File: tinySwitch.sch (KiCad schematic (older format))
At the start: 8 parts, among them J1 Vout Vin Gnd, J2 Raspberry Pi Input, K1 1 Channel Relay, SW1 Power Button, U1 Digispark Tiny85

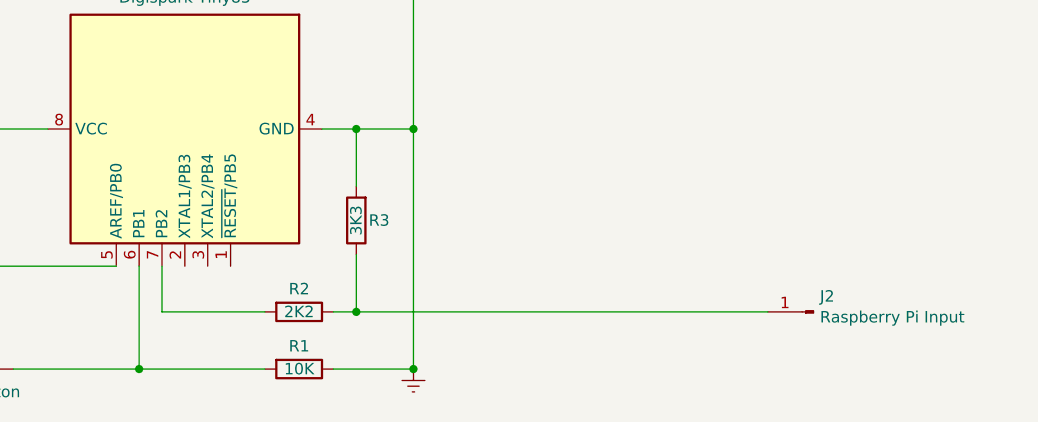
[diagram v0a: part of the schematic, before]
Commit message: Adding RPi detection line (Input)
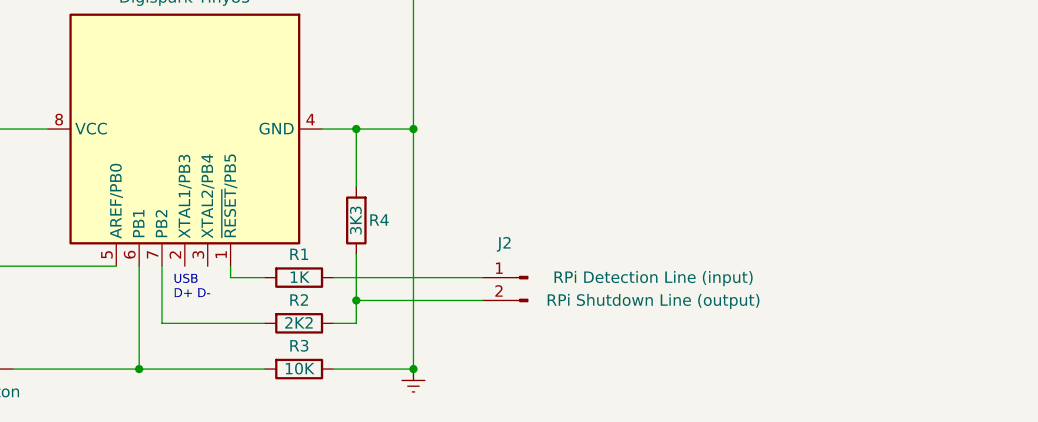
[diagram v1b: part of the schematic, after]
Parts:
- removed J2: Raspberry Pi Input, symbol Connector:Conn_01x01_Male
- added J2: Conn_01x02_Male, symbol Connector:Conn_01x02_Male
- added R1: 1K, symbol Device:R
- renumbered R1 to R3, R3 to R4
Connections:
- net at U1.1 (~RESET~/PB5): now also R1.2
- net at R2.1, R4.1: now also J2.2 (Pin_2)
- new net: J2.1 (Pin_1), R1.1
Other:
- note added: "USB\nD+ D-"
- moved on the sheet: R2
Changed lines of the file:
@@
 $EndComp
 $Comp
-L Device:R R1
+L Device:R R3
 U 1 1 5FBB20BE
 P 6600 4400
-F 0 "R1" V 6500 4400 50  0000 C CNN
+F 0 "R3" V 6500 4400 50  0000 C CNN
 F 1 "10K" V 6600 4400 50  0000 C CNN
 F 2 "" V 6530 4400 50  0001 C CNN
@@
 Connection ~ 7100 3350
 Wire Wire Line
-	6000 3950 6000 4150
+	6000 3950 6000 4200
 Wire Wire Line
-	6000 4150 6450 4150
+	6000 4200 6450 4200
 $Comp
 L Device:R R2
 U 1 1 5FBBB646
-P 6600 4150
-F 0 "R2" V 6500 4150 50  0000 C CNN
-F 1 "2K2" V 6600 4150 50  0000 C CNN
-F 2 "" V 6530 4150 50  0001 C CNN
-F 3 "~" H 6600 4150 50  0001 C CNN
-	1    6600 4150
+P 6600 4200
+F 0 "R2" V 6500 4200 50  0000 C CNN
+F 1 "2K2" V 6600 4200 50  0000 C CNN
+F 2 "" V 6530 4200 50  0001 C CNN
+F 3 "~" H 6600 4200 50  0001 C CNN
+	1    6600 4200
 	0    1    1    0
 $EndComp
 $Comp
-L Device:R R3
+L Device:R R4
 U 1 1 5FBBD94C
 P 6850 3750
-F 0 "R3" H 6750 3750 50  0000 C CNN
+F 0 "R4" H 6750 3750 50  0000 C CNN
 F 1 "3K3" V 6850 3750 50  0000 C CNN
 F 2 "" V 6780 3750 50  0001 C CNN
@@
 	6850 3350 6700 3350
 Wire Wire Line
-	6750 4150 6850 4150
+	6750 4200 6850 4200
 Wire Wire Line
-	6850 4150 6850 3900
-Connection ~ 6850 4150
-$Comp
-L Connector:Conn_01x01_Male J2
-U 1 1 5FBC60A1
-P 8850 4150
-F 0 "J2" H 8822 4082 50  0000 R CNN
-F 1 "Raspberry Pi Input" H 8822 4173 50  0000 R CNN
-F 2 "" H 8850 4150 50  0001 C CNN
-F 3 "~" H 8850 4150 50  0001 C CNN
-	1    8850 4150
-	-1   0    0    1
-$EndComp
+	6850 4200 6850 4100
 $Comp
 L Connector:Conn_01x03_Male J1
@@
 	0    1    1    0
 $EndComp
+$Comp
+L Connector:Conn_01x02_Male J2
+U 1 1 5FBBFAF0
+P 7600 4000
+F 0 "J2" H 7700 4150 50  0000 C CNN
+F 1 "Conn_01x02_Male" H 7708 4090 50  0001 C CNN
+F 2 "" H 7600 4000 50  0001 C CNN
+F 3 "~" H 7600 4000 50  0001 C CNN
+F 4 "RPi Detection Line (input)" H 7050 4000 50  0000 C CNN "Input"
+F 5 "RPi Shutdown Line (output)" H 7050 3900 50  0000 C CNN "Output"
+	1    7600 4000
+	-1   0    0    -1
+$EndComp
+$Comp
+L Device:R R1
+U 1 1 5FBC97E0
+P 6600 4000
+F 0 "R1" V 6500 4000 50  0000 C CNN
+F 1 "1K" V 6600 4000 50  0000 C CNN
+F 2 "" V 6530 4000 50  0001 C CNN
+F 3 "~" H 6600 4000 50  0001 C CNN
+	1    6600 4000
+	0    1    1    0
+$EndComp
 Wire Wire Line
-	6850 4150 8650 4150
+	6450 4000 6300 4000
+Wire Wire Line
+	6300 4000 6300 3950
+Text Notes 6050 4100 0    39   ~ 0
+ USB\nD+ D-
+Wire Wire Line
+	7400 4100 6850 4100
+Connection ~ 6850 4100
+Wire Wire Line
+	6850 4100 6850 3900
+Wire Wire Line
+	6750 4000 7400 4000
 $EndSCHEMATC

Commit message: Hardware revision v1.1
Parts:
- removed J1: Vout Vin Gnd, symbol Connector:Conn_01x03_Male
- removed J2: Conn_01x02_Male, symbol Connector:Conn_01x02_Male
- added J1: Conn_01x03, symbol Connector_Generic:Conn_01x03
- added J2: Conn_01x02, symbol Connector_Generic:Conn_01x02
- renumbered R4 to R1, R1 to R3, R3 to R4
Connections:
- net Earth: now also J1.3 (Pin_3)
- net at U1.1 (~RESET~/PB5): no longer R3.2
- net at U1.3 (XTAL2/PB4): now also R2.2
- net at U1.7 (PB2): now also R3.2; no longer R2.2
- net at K1.1, K1.13, K1.14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: now also J1.2 (Pin_2)
- net at K1.7, K1.8: now also J1.1 (Pin_1)
- net at R1.1, R2.1: now also J2.1 (Pin_1)
- net at R3.1: now also J2.2 (Pin_2)
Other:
- moved on the sheet: R2, R3, R4, SW1
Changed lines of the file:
@@
 Sheet 1 1
 Title "tinySwitch"
-Date "2020-11-22"
-Rev "1.0"
+Date "2020-11-26"
+Rev "1.1"
 Comp "Ben"
-Comment1 "ON/OFF switch for raspberry"
-Comment2 ""
+Comment1 ""
+Comment2 "Tiny85 USB with 1 channel relay"
 Comment3 ""
-Comment4 ""
+Comment4 "ON/OFF switch for Raspberry Pi"
 $EndDescr
 $Comp
@@
 L Switch:SW_Push SW1
 U 1 1 5FBAA7A8
-P 5150 4400
-F 0 "SW1" H 5150 4550 50  0000 C CNN
-F 1 "Power Button" H 5150 4300 50  0000 C CNN
-F 2 "" H 5150 4600 50  0001 C CNN
-F 3 "~" H 5150 4600 50  0001 C CNN
-	1    5150 4400
-	1    0    0    -1
-$EndComp
-Wire Wire Line
-	4950 4400 4950 3350
+P 5150 4450
+F 0 "SW1" H 5150 4650 50  0000 C CNN
+F 1 "Power Button" H 5150 4350 50  0000 C CNN
+F 2 "" H 5150 4650 50  0001 C CNN
+F 3 "~" H 5150 4650 50  0001 C CNN
+	1    5150 4450
+	1    0    0    -1
+$EndComp
+Wire Wire Line
+	4950 4450 4950 3350
 Connection ~ 4950 3350
 Wire Wire Line
 	4950 3350 5500 3350
 Wire Wire Line
-	5350 4400 5900 4400
-Wire Wire Line
-	5900 4400 5900 3950
+	5350 4450 5900 4450
+Wire Wire Line
+	5900 4450 5900 3950
 $Comp
 L power:Earth #PWR?
@@
 L power:Earth #PWR?
 U 1 1 5FBB0448
-P 7100 4400
-F 0 "#PWR?" H 7100 4150 50  0001 C CNN
-F 1 "Earth" H 7100 4250 50  0001 C CNN
-F 2 "" H 7100 4400 50  0001 C CNN
-F 3 "~" H 7100 4400 50  0001 C CNN
-	1    7100 4400
-	1    0    0    -1
-$EndComp
-$Comp
-L Device:R R3
+P 7100 4550
+F 0 "#PWR?" H 7100 4300 50  0001 C CNN
+F 1 "Earth" H 7100 4400 50  0001 C CNN
+F 2 "" H 7100 4550 50  0001 C CNN
+F 3 "~" H 7100 4550 50  0001 C CNN
+	1    7100 4550
+	1    0    0    -1
+$EndComp
+$Comp
+L Device:R R4
 U 1 1 5FBB20BE
-P 6600 4400
-F 0 "R3" V 6500 4400 50  0000 C CNN
-F 1 "10K" V 6600 4400 50  0000 C CNN
-F 2 "" V 6530 4400 50  0001 C CNN
-F 3 "~" H 6600 4400 50  0001 C CNN
-	1    6600 4400
+P 6600 4450
+F 0 "R4" V 6500 4450 50  0000 C CNN
+F 1 "10K" V 6600 4450 50  0000 C CNN
+F 2 "" V 6530 4450 50  0001 C CNN
+F 3 "~" H 6600 4450 50  0001 C CNN
+	1    6600 4450
 	0    1    1    0
 $EndComp
 Wire Wire Line
-	5900 4400 6450 4400
-Connection ~ 5900 4400
-Wire Wire Line
-	6750 4400 7100 4400
-Wire Wire Line
-	7100 4400 7100 3350
+	5900 4450 6450 4450
+Connection ~ 5900 4450
+Wire Wire Line
+	6750 4450 7100 4450
+Wire Wire Line
+	7100 4450 7100 3350
 Wire Wire Line
 	7100 3350 6850 3350
-Connection ~ 7100 4400
+Connection ~ 7100 4450
 Wire Wire Line
 	4950 3350 4950 2950
@@
 	4950 2950 4700 2950
 Wire Wire Line
-	4950 2950 4950 2050
-Wire Wire Line
-	4950 2050 4450 2050
-Wire Wire Line
-	4450 2050 4450 1250
+	4950 2950 4950 2450
+Wire Wire Line
+	4950 2450 4450 2450
+Wire Wire Line
+	4450 2450 4450 2200
 Connection ~ 4950 2950
 Wire Wire Line
 	4100 2950 4000 2950
 Wire Wire Line
-	4000 2950 4000 2050
-Wire Wire Line
-	4000 2050 4350 2050
-Wire Wire Line
-	4350 2050 4350 1250
-Wire Wire Line
-	7100 3350 7100 1950
-Wire Wire Line
-	7100 1950 4550 1950
-Wire Wire Line
-	4550 1950 4550 1250
+	4000 2950 4000 2450
+Wire Wire Line
+	4000 2450 4350 2450
+Wire Wire Line
+	4350 2450 4350 2200
+Wire Wire Line
+	7100 3350 7100 2350
+Wire Wire Line
+	7100 2350 4550 2350
+Wire Wire Line
+	4550 2350 4550 2200
 Connection ~ 7100 3350
 Wire Wire Line
-	6000 3950 6000 4200
-Wire Wire Line
-	6000 4200 6450 4200
+	6000 3950 6000 4250
+Wire Wire Line
+	6000 4250 6450 4250
 $Comp
 L Device:R R2
 U 1 1 5FBBB646
-P 6600 4200
-F 0 "R2" V 6500 4200 50  0000 C CNN
-F 1 "2K2" V 6600 4200 50  0000 C CNN
-F 2 "" V 6530 4200 50  0001 C CNN
-F 3 "~" H 6600 4200 50  0001 C CNN
-	1    6600 4200
+P 6600 4050
+F 0 "R2" V 6500 4050 50  0000 C CNN
+F 1 "2K2" V 6600 4050 50  0000 C CNN
+F 2 "" V 6530 4050 50  0001 C CNN
+F 3 "~" H 6600 4050 50  0001 C CNN
+	1    6600 4050
 	0    1    1    0
 $EndComp
 $Comp
-L Device:R R4
+L Device:R R1
 U 1 1 5FBBD94C
 P 6850 3750
-F 0 "R4" H 6750 3750 50  0000 C CNN
+F 0 "R1" H 6750 3750 50  0000 C CNN
 F 1 "3K3" V 6850 3750 50  0000 C CNN
 F 2 "" V 6780 3750 50  0001 C CNN
@@
 Wire Wire Line
 	6850 3350 6700 3350
-Wire Wire Line
-	6750 4200 6850 4200
-Wire Wire Line
-	6850 4200 6850 4100
-$Comp
-L Connector:Conn_01x03_Male J1
-U 1 1 5FBC4F8A
-P 4450 1050
-F 0 "J1" V 4250 1050 50  0000 C CNN
-F 1 "Vout Vin Gnd" V 4400 1050 50  0000 C CNN
-F 2 "" H 4450 1050 50  0001 C CNN
-F 3 "~" H 4450 1050 50  0001 C CNN
-	1    4450 1050
+$Comp
+L Device:R R3
+U 1 1 5FBC97E0
+P 6600 4250
+F 0 "R3" V 6500 4250 50  0000 C CNN
+F 1 "1K" V 6600 4250 50  0000 C CNN
+F 2 "" V 6530 4250 50  0001 C CNN
+F 3 "~" H 6600 4250 50  0001 C CNN
+	1    6600 4250
 	0    1    1    0
 $EndComp
-$Comp
-L Connector:Conn_01x02_Male J2
-U 1 1 5FBBFAF0
-P 7600 4000
-F 0 "J2" H 7700 4150 50  0000 C CNN
-F 1 "Conn_01x02_Male" H 7708 4090 50  0001 C CNN
-F 2 "" H 7600 4000 50  0001 C CNN
-F 3 "~" H 7600 4000 50  0001 C CNN
-F 4 "RPi Detection Line (input)" H 7050 4000 50  0000 C CNN "Input"
-F 5 "RPi Shutdown Line (output)" H 7050 3900 50  0000 C CNN "Output"
-	1    7600 4000
-	-1   0    0    -1
-$EndComp
-$Comp
-L Device:R R1
-U 1 1 5FBC97E0
-P 6600 4000
-F 0 "R1" V 6500 4000 50  0000 C CNN
-F 1 "1K" V 6600 4000 50  0000 C CNN
-F 2 "" V 6530 4000 50  0001 C CNN
-F 3 "~" H 6600 4000 50  0001 C CNN
-	1    6600 4000
-	0    1    1    0
-$EndComp
-Wire Wire Line
-	6450 4000 6300 4000
-Wire Wire Line
-	6300 4000 6300 3950
-Text Notes 6050 4100 0    39   ~ 0
+Wire Wire Line
+	6450 4050 6200 4050
+Wire Wire Line
+	6200 4050 6200 3950
+Text Notes 6050 3400 0    39   ~ 0
  USB\nD+ D-
 Wire Wire Line
-	7400 4100 6850 4100
-Connection ~ 6850 4100
-Wire Wire Line
-	6850 4100 6850 3900
-Wire Wire Line
-	6750 4000 7400 4000
+	6750 4050 6850 4050
+Wire Wire Line
+	6850 4050 6850 3900
+Connection ~ 6850 4050
+Wire Wire Line
+	6850 4050 7400 4050
+Wire Wire Line
+	6750 4250 6850 4250
+Wire Wire Line
+	6850 4250 6850 4150
+Wire Wire Line
+	6850 4150 7400 4150
+Wire Wire Line
+	7100 4450 7100 4550
+$Comp
+L Connector_Generic:Conn_01x02 J2
+U 1 1 5FC1178B
+P 7600 4050
+F 0 "J2" H 7550 4200 50  0000 L CNN
+F 1 "Conn_01x02" H 7680 4042 50  0001 L CNN
+F 2 "" H 7600 4050 50  0001 C CNN
+F 3 "~" H 7600 4050 50  0001 C CNN
+F 4 "RPi Shutdown Line (output)" H 7700 4050 50  0000 L CNN "Output"
+F 5 "RPi Detection Line (input) " H 7700 3950 50  0000 L CNN "Input"
+	1    7600 4050
+	1    0    0    -1
+$EndComp
+$Comp
+L Connector_Generic:Conn_01x03 J1
+U 1 1 5FC158BD
+P 4450 2000
+F 0 "J1" V 4650 2050 50  0000 R CNN
+F 1 "Conn_01x03" H 4530 1951 50  0001 L CNN
+F 2 "" H 4450 2000 50  0001 C CNN
+F 3 "~" H 4450 2000 50  0001 C CNN
+F 4 "Vout" V 4550 2250 50  0000 R CNN "vout"
+F 5 "Vin" V 4550 2050 50  0000 R CNN "vin"
+F 6 "Gnd" V 4550 1900 50  0000 R CNN "gnd"
+	1    4450 2000
+	0    -1   -1   0
+$EndComp
 $EndSCHEMATC

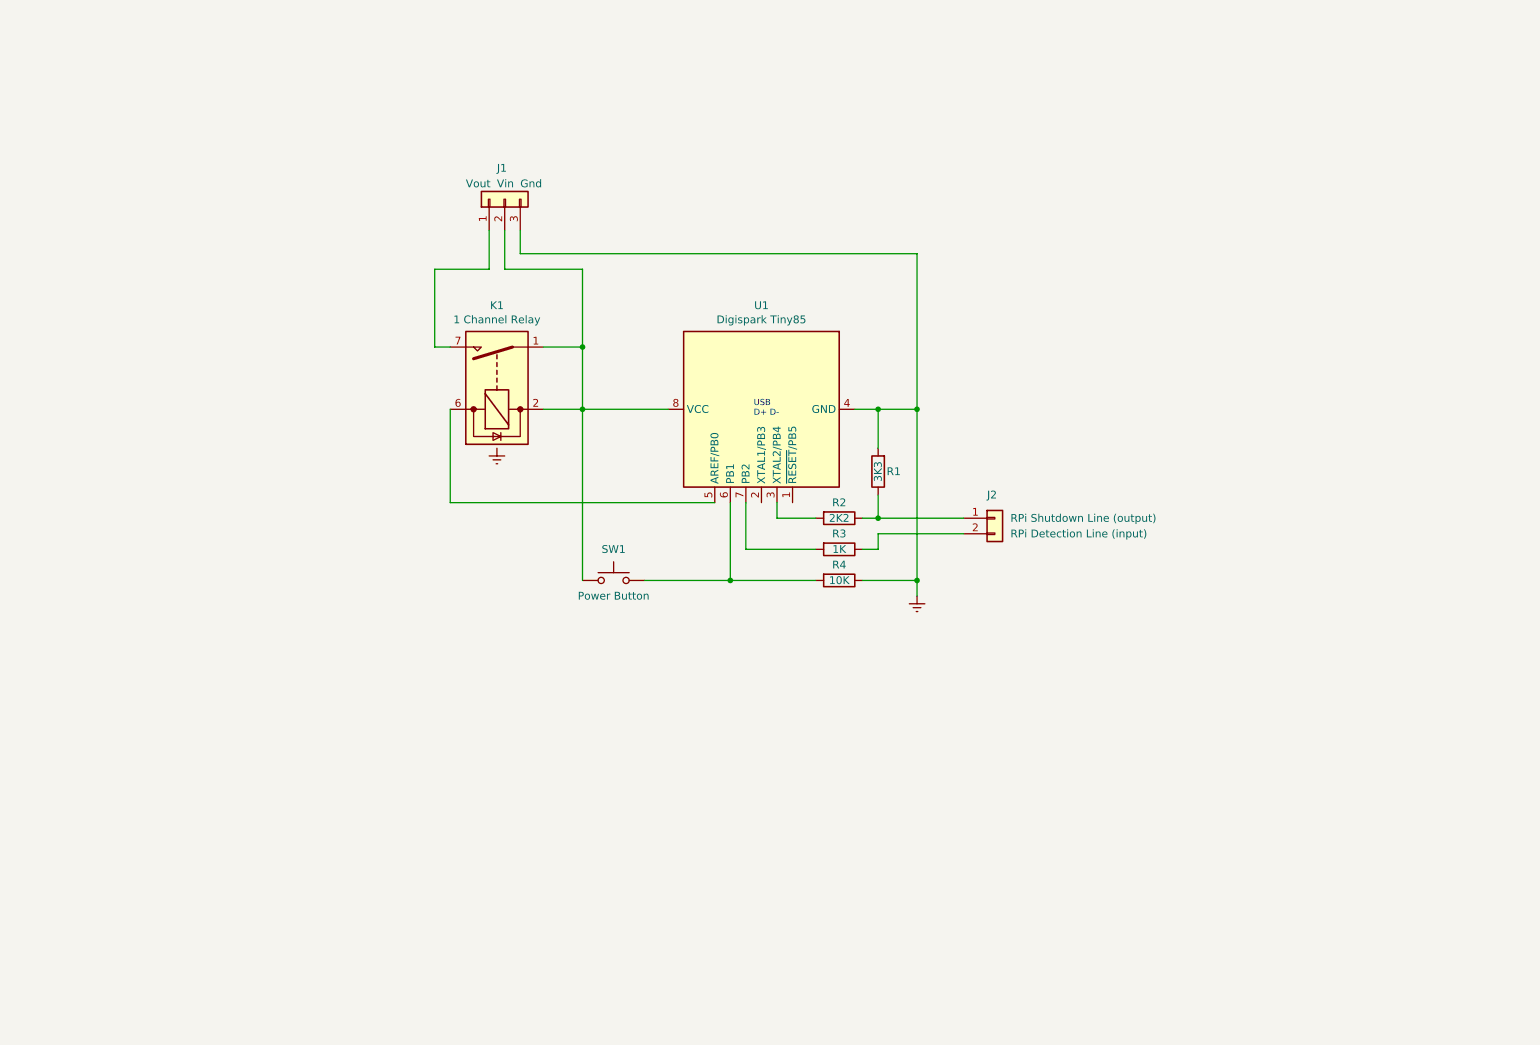
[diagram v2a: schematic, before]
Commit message: New schematics with ext connections
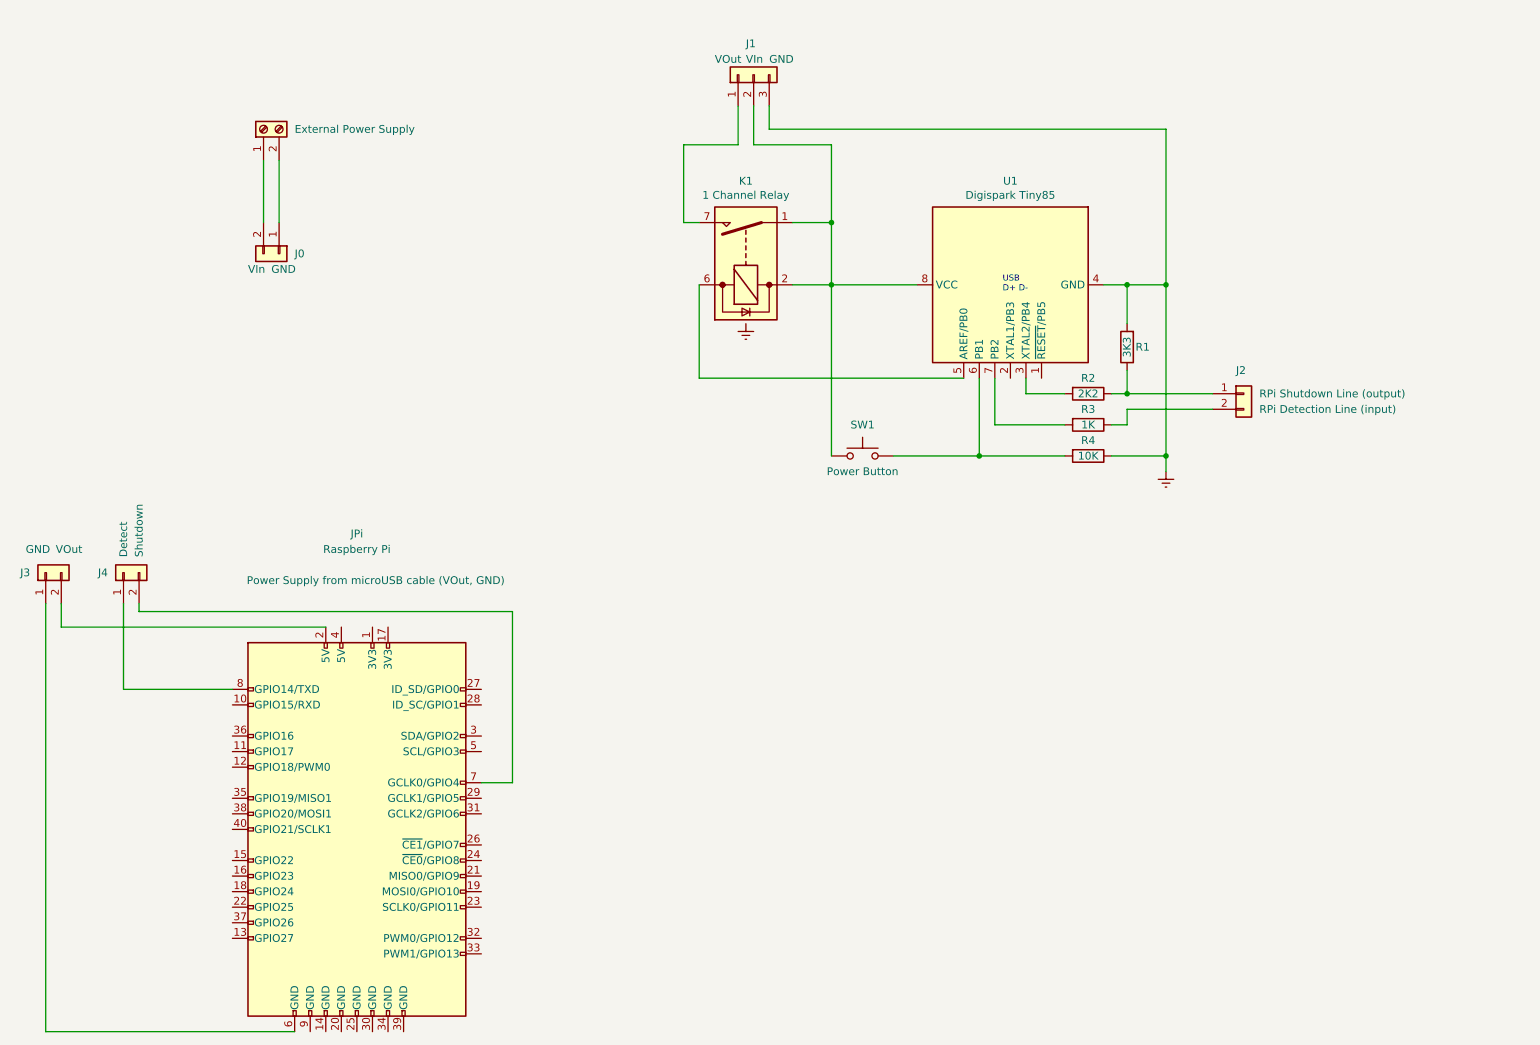
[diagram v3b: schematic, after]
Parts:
- added J0, J3, J4: Conn_01x02, symbol Connector_Generic:Conn_01x02
- added J?: External Power Supply, symbol Connector:Screw_Terminal_01x02
- added JPi: Raspberry Pi, symbol Connector:Raspberry_Pi_2_3
- J1: gnd Gnd -> GND; vin Vin -> VIn; vout Vout -> VOut
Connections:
- new net: J3.2 (Pin_2), JPi.2 (5V)
- new net: J3.1 (Pin_1), JPi.6 (GND)
- new net: J4.2 (Pin_2), JPi.7 (GCLK0/GPIO4)
- new net: J4.1 (Pin_1), JPi.8 (GPIO14/TXD)
- new net: J0.1 (Pin_1), J?.2 (Pin_2)
- new net: J0.2 (Pin_2), J?.1 (Pin_1)
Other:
- moved on the sheet: J1, J2, K1, R1, R2, R3, R4, SW1, U1

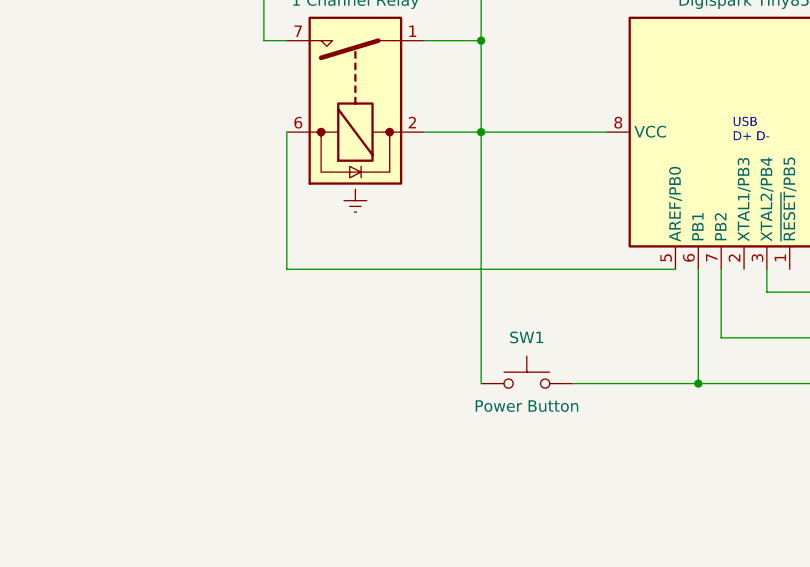
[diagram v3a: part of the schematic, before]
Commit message: signal to toggle relay
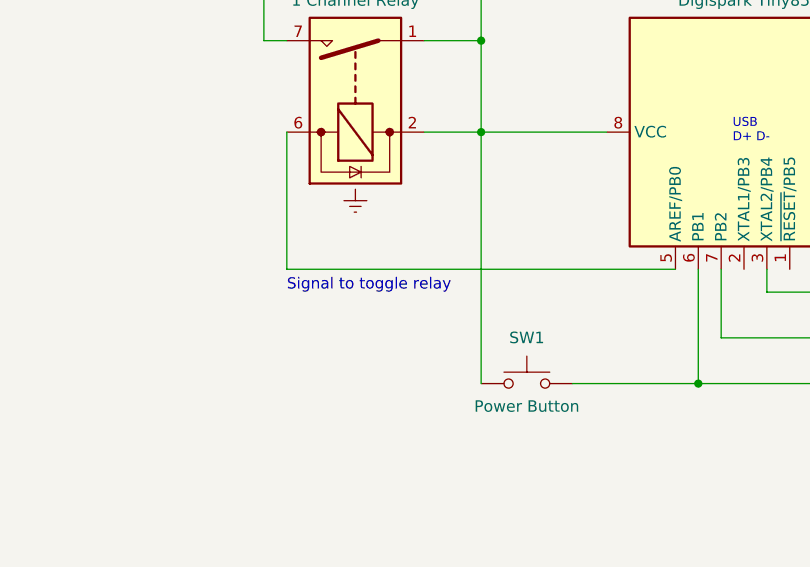
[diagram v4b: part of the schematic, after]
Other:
- note added: "Signal to toggle relay"
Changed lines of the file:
@@
 Wire Wire Line
 	3000 1750 3000 2150
+Text Notes 5700 3250 0    49   ~ 0
+Signal to toggle relay
 $EndSCHEMATC
